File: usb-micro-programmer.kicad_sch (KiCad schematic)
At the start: 38 parts, among them J1 USB_B_Micro, J2 ESP_Link, J3 ESP_Prog, J4 Standard_Prog, Q1 S8050(NPN), Q2 S8050(NPN), U1 CH340C/G, U2 AMS1117-3.3, Y1 12MHz

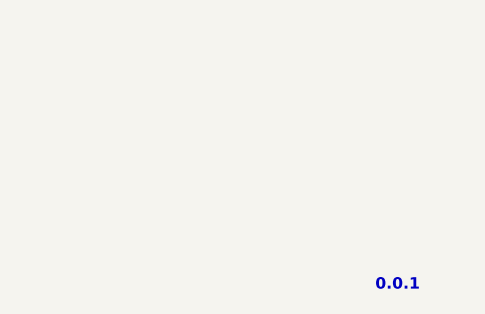
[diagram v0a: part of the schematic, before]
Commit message: Correcting changes based on gerbers
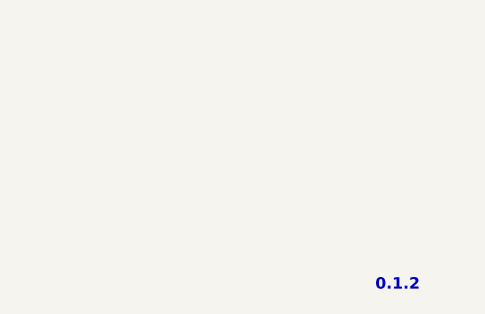
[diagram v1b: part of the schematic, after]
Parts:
- Q1, Q2: footprint digikey-footprints:SOT-23-3 -> Package_TO_SOT_SMD:SOT-23
- SW_EN1, SW_IO0: footprint Button_Switch_THT:SW_PUSH_6mm_H9.5mm -> Button_Switch_THT:SW_PUSH_6mm_H5mm
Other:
- note added: "0.1.2"
- note removed: "0.0.1"
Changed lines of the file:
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@@
     (effects (font (size 2.54 2.54)) (justify left bottom))
   )
-  (text "0.0.1" (at 269.24 194.31 0)
+  (text "0.1.2" (at 269.24 194.31 0)
     (effects (font (size 1.27 1.27) bold) (justify left bottom))
   )
@@
     (property "Reference" "SW_EN1" (id 0) (at 236.22 45.72 0))
     (property "Value" "SW_Push" (id 1) (at 236.22 48.26 0))
-    (property "Footprint" "Button_Switch_THT:SW_PUSH_6mm_H9.5mm" (id 2) (at 236.22 48.26 0)
+    (property "Footprint" "Button_Switch_THT:SW_PUSH_6mm_H5mm" (id 2) (at 236.22 48.26 0)
       (effects (font (size 1.27 1.27)) hide)
     )
@@
       (effects (font (size 1.25 1.25)) (justify left))
     )
-    (property "Footprint" "digikey-footprints:SOT-23-3" (id 2) (at 214.63 68.58 0)
+    (property "Footprint" "Package_TO_SOT_SMD:SOT-23" (id 2) (at 214.63 68.58 0)
       (effects (font (size 1.524 1.524)) (justify left) hide)
     )
@@
     (property "Reference" "SW_IO0" (id 0) (at 260.35 45.72 0))
     (property "Value" "SW_Push" (id 1) (at 260.35 48.26 0))
-    (property "Footprint" "Button_Switch_THT:SW_PUSH_6mm_H9.5mm" (id 2) (at 260.35 48.26 0)
+    (property "Footprint" "Button_Switch_THT:SW_PUSH_6mm_H5mm" (id 2) (at 260.35 48.26 0)
       (effects (font (size 1.27 1.27)) hide)
     )
@@
       (effects (font (size 1.25 1.25)) (justify left))
     )
-    (property "Footprint" "digikey-footprints:SOT-23-3" (id 2) (at 214.63 44.45 0)
+    (property "Footprint" "Package_TO_SOT_SMD:SOT-23" (id 2) (at 214.63 44.45 0)
       (effects (font (size 1.524 1.524)) (justify left) hide)
     )
@@
     )
     (path "/e7ea1b42-2c9c-4cae-a6c5-4833d7969518"
-      (reference "Q1") (unit 1) (value "S8050(NPN)") (footprint "digikey-footprints:SOT-23-3")
+      (reference "Q1") (unit 1) (value "S8050(NPN)") (footprint "Package_TO_SOT_SMD:SOT-23")
     )
     (path "/6b2627d4-5f4a-4048-8263-3fc729e0bc60"
-      (reference "Q2") (unit 1) (value "S8050(NPN)") (footprint "digikey-footprints:SOT-23-3")
+      (reference "Q2") (unit 1) (value "S8050(NPN)") (footprint "Package_TO_SOT_SMD:SOT-23")
     )
     (path "/2deabaae-7edf-4a32-a9e1-9736e5e5c34d"
@@
     )
     (path "/05f203ad-2a00-4fbe-88d6-e9acb198cc0b"
-      (reference "SW_EN1") (unit 1) (value "SW_Push") (footprint "Button_Switch_THT:SW_PUSH_6mm_H9.5mm")
+      (reference "SW_EN1") (unit 1) (value "SW_Push") (footprint "Button_Switch_THT:SW_PUSH_6mm_H5mm")
     )
     (path "/d869546a-7439-4f9c-b440-c359ba781432"
-      (reference "SW_IO0") (unit 1) (value "SW_Push") (footprint "Button_Switch_THT:SW_PUSH_6mm_H9.5mm")
+      (reference "SW_IO0") (unit 1) (value "SW_Push") (footprint "Button_Switch_THT:SW_PUSH_6mm_H5mm")
     )
     (path "/09ab9b2a-26ef-4942-ba61-f8a6673867aa"

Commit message: Adding changes of Rev 0.1.4
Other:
- note added: "0.1.4"
- note removed: "0.1.2"
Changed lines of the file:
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@@
     (effects (font (size 2.54 2.54)) (justify left bottom))
   )
-  (text "0.1.2" (at 269.24 194.31 0)
+  (text "0.1.4" (at 269.24 194.31 0)
     (effects (font (size 1.27 1.27) bold) (justify left bottom))
   )
